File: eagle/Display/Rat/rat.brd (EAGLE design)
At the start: 97.8 x 101.3 mm, 67 parts, among them IC1 4511D, IC2 MEGA128-A, IC3 PCA82C250T, IC4 74LS138D, IC5 74LS138D, IC6 LM3914V, IC7 LM3914V, Q1 18.4320 MHz

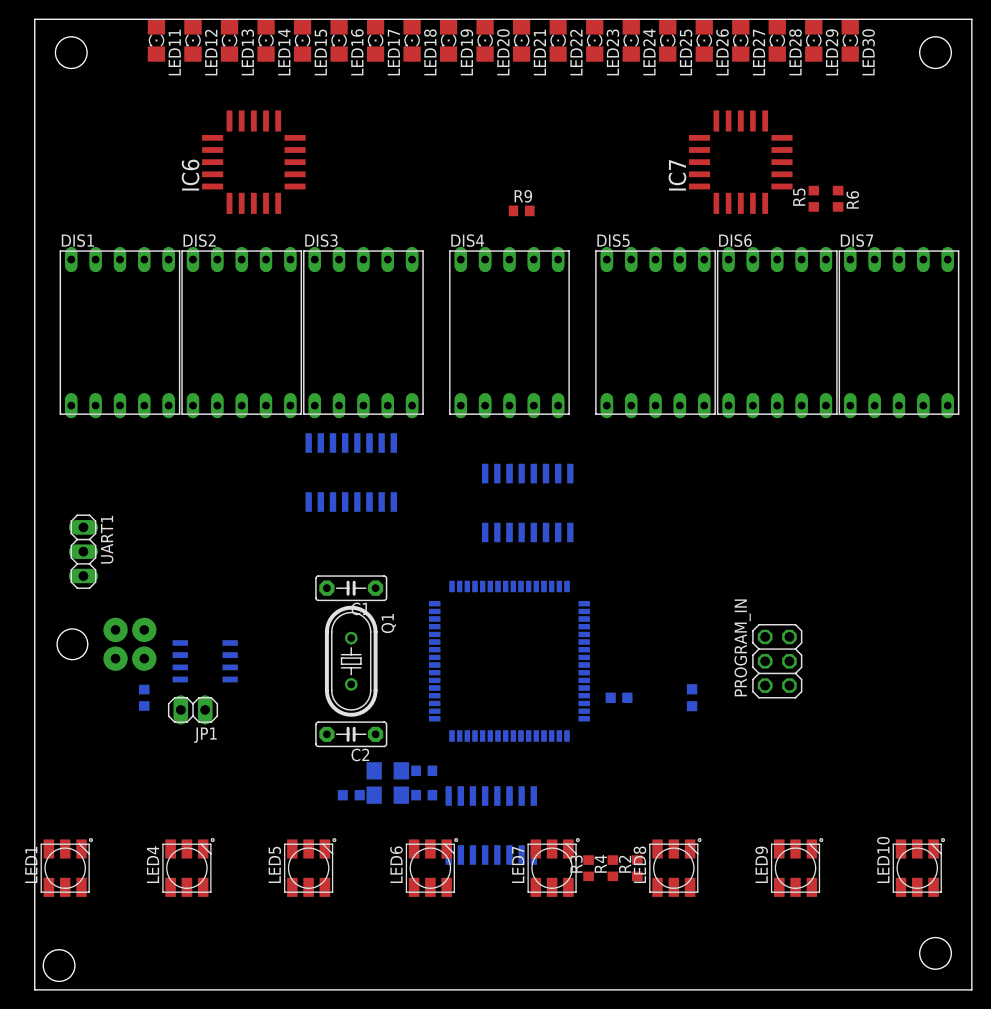
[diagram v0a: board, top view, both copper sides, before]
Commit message: changes to the schematic and board layout
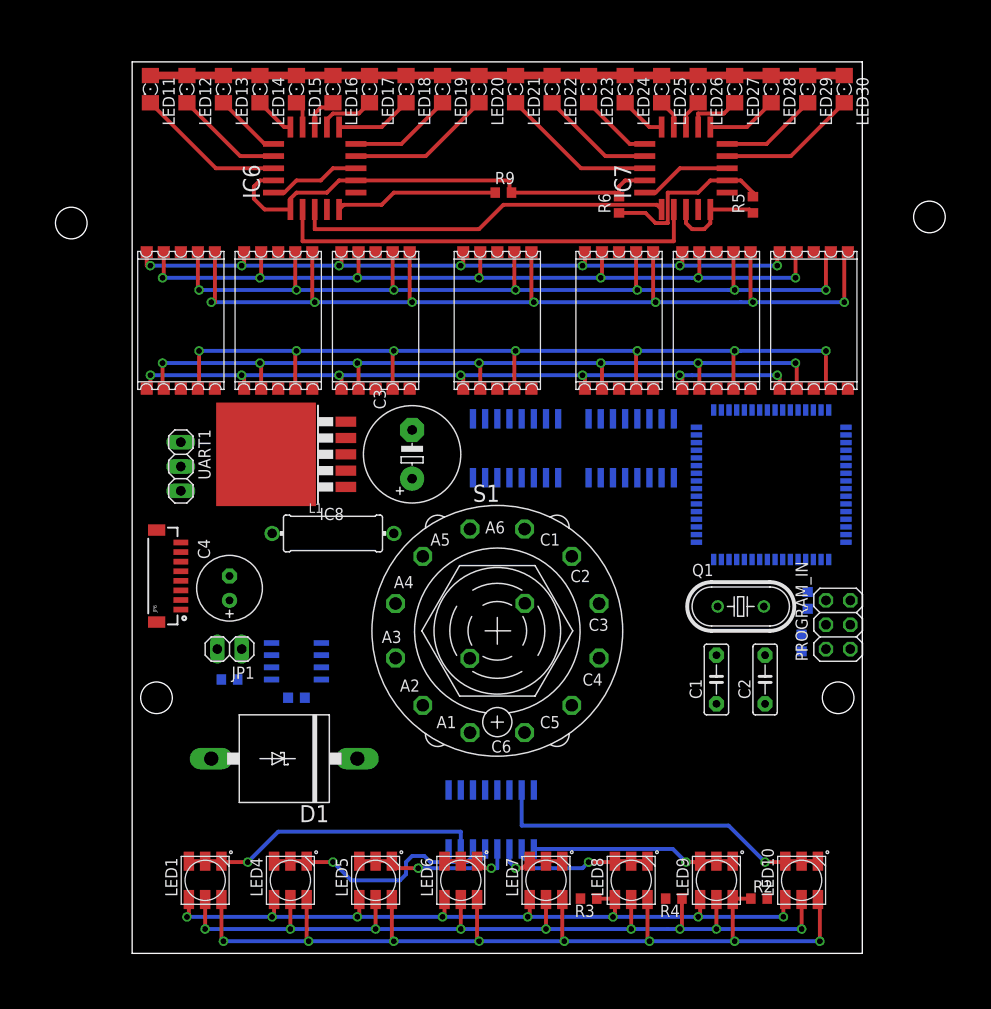
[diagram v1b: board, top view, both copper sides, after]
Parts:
- removed DIS1, DIS2, DIS3, DIS4, DIS5, DIS6, DIS7: HD-H103, display-hp:HDSP-M
- removed LED2, LED3: GREEN, led:1206
- removed R7, R8: 200, rcl:R0603
- removed U$1: MICROFIT4, UNICORN:MICROFIT4SOCK
- added C3: 680 uf, rcl:E5-10,5
- added C4: 220 uf, rcl:E2,5-7
- added D1: 1n5824, diode:P6T15
- added IC8: (no value), linear:TO263-5
- added JP6: (no value), SparkFun-Connectors:BM08B-SRSS-TB
- added L1: 33 uf, rcl:TFI0410
- added S1: (no value), switch:CK102X06
- added U$2, U$3, U$4, U$5, U$6, U$7, U$8: REDSEVENSEGMENT, red_segment:REDSEGMENT
- moved C2 43.6 mm to (95.2, 41.3), turned to 90 degrees
- moved Q1 41.0 mm to (92.7, 48.9), turned to 0 degrees
- moved C1 39.3 mm to (90.2, 41.3), turned to 90 degrees
- moved IC2 32.9 mm to (95.9, 61.6), turned to 0 degrees
- moved JP3 29.7 mm to (31.8, 39.4)
- moved JP2 28.5 mm to (102.9, 39.4)
- moved R6 22.9 mm to (80.0, 90.8), turned to 90 degrees
- moved C19 22.2 mm to (99.7, 49.5), turned to 270 degrees
- moved JP5 17.8 mm to (22.9, 88.9)
- moved IC4 17.3 mm to (69.2, 65.4)
- moved JP4 17.2 mm to (112.4, 89.5)
- moved LED1 14.7 mm to (36.8, 20.3)
- moved UART1 13.5 mm to (34.3, 63.5)
- moved R2 13.1 mm to (94.6, 18.4), turned to 0 degrees
- moved C6 12.8 mm to (99.1, 45.1)
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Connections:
- removed net N$11: LED3.A, R7.1
- removed net N$4: IC2.16, R8.2
- removed net N$5: IC2.15, R7.2
- removed net N$7: LED2.A, R8.1
- new net N$45: D1.C, IC8.2, L1.1
- new net VCC: C3.+, IC8.1, JP6.5, JP6.6
- net +5V: now also C4.+, IC8.4, L1.2
- net CANJUMP1: now also JP6.1; no longer U$1.PIN1
- net N$12: now also U$2.D, U$3.D, U$4.D, U$5.D, U$6.D, U$7.D, U$8.D; no longer DIS1.2, DIS2.2, DIS3.2, DIS4.2, DIS5.2, DIS6.2, DIS7.2
- net N$13: now also U$2.E, U$3.E, U$4.E, U$5.E, U$6.E, U$7.E, U$8.E; no longer DIS1.1, DIS2.1, DIS3.1, DIS4.1, DIS5.1, DIS6.1, DIS7.1
- net N$14: now also U$2.F, U$3.F, U$4.F, U$5.F, U$6.F, U$7.F, U$8.F; no longer DIS1.9, DIS2.9, DIS3.9, DIS4.9, DIS5.9, DIS6.9, DIS7.9
- net N$15: now also U$2.G, U$3.G, U$4.G, U$5.G, U$6.G, U$7.G, U$8.G; no longer DIS1.10, DIS2.10, DIS3.10, DIS4.10, DIS5.10, DIS6.10, DIS7.10
- net N$16: now also U$2.GN, U$2.GND; no longer DIS1.3, DIS1.8
- net N$17: now also U$3.GN, U$3.GND; no longer DIS2.3, DIS2.8
- net N$18: now also U$4.GN, U$4.GND; no longer DIS3.3, DIS3.8
- net N$19: now also U$5.GN, U$5.GND; no longer DIS4.3, DIS4.8
- net N$20: now also U$6.GN, U$6.GND; no longer DIS5.3, DIS5.8
- net N$21: now also U$7.GN, U$7.GND; no longer DIS6.3, DIS6.8
- net N$22: now also U$8.GN, U$8.GND; no longer DIS7.3, DIS7.8
- net N$3: now also U$2.A, U$3.A, U$4.A, U$5.A, U$6.A, U$7.A, U$8.A; no longer DIS1.7, DIS2.7, DIS3.7, DIS4.7, DIS5.7, DIS6.7, DIS7.7
- net N$51: now also JP6.2; no longer U$1.PIN2
- net N$6: now also U$2.B, U$3.B, U$4.B, U$5.B, U$6.B, U$7.B, U$8.B; no longer DIS1.6, DIS2.6, DIS3.6, DIS4.6, DIS5.6, DIS6.6, DIS7.6
- net N$8: now also U$2.C, U$3.C, U$4.C, U$5.C, U$6.C, U$7.C, U$8.C; no longer DIS1.4, DIS2.4, DIS3.4, DIS4.4, DIS5.4, DIS6.4, DIS7.4
- net PE: now also C3.-, C4.-, D1.A, IC8.3, IC8.5, IC8.6, JP6.3, JP6.4; no longer LED2.C, LED3.C, U$1.PIN3, U$1.PIN4
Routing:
- net N$6: track 0.00 -> 104.5 mm, vias 0 -> 7
- net N$32: track 0.00 -> 99.6 mm, vias 0 -> 8
- net N$8: track 0.00 -> 94.2 mm, vias 0 -> 7
- net N$3: track 0.00 -> 94.2 mm, vias 0 -> 7
- net N$30: track 0.00 -> 90.1 mm, vias 0 -> 9
- net N$12: track 0.00 -> 85.6 mm, vias 0 -> 7
- net N$14: track 0.00 -> 85.6 mm, vias 0 -> 7
- net N$31: track 0.00 -> 79.3 mm, vias 0 -> 8
- net N$15: track 0.00 -> 77.1 mm, vias 0 -> 7
- net N$13: track 0.00 -> 77.1 mm, vias 0 -> 7
- net N$69: track 0.00 -> 72.4 mm
- net PE: track 0.00 -> 49.3 mm
- net N$73: track 0.00 -> 45.4 mm
- net N$72: track 0.00 -> 39.5 mm
- net N$40: track 0.00 -> 36.2 mm, vias 0 -> 1
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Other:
- board size 97.8 x 101.3 mm -> 76.2 x 93 mm

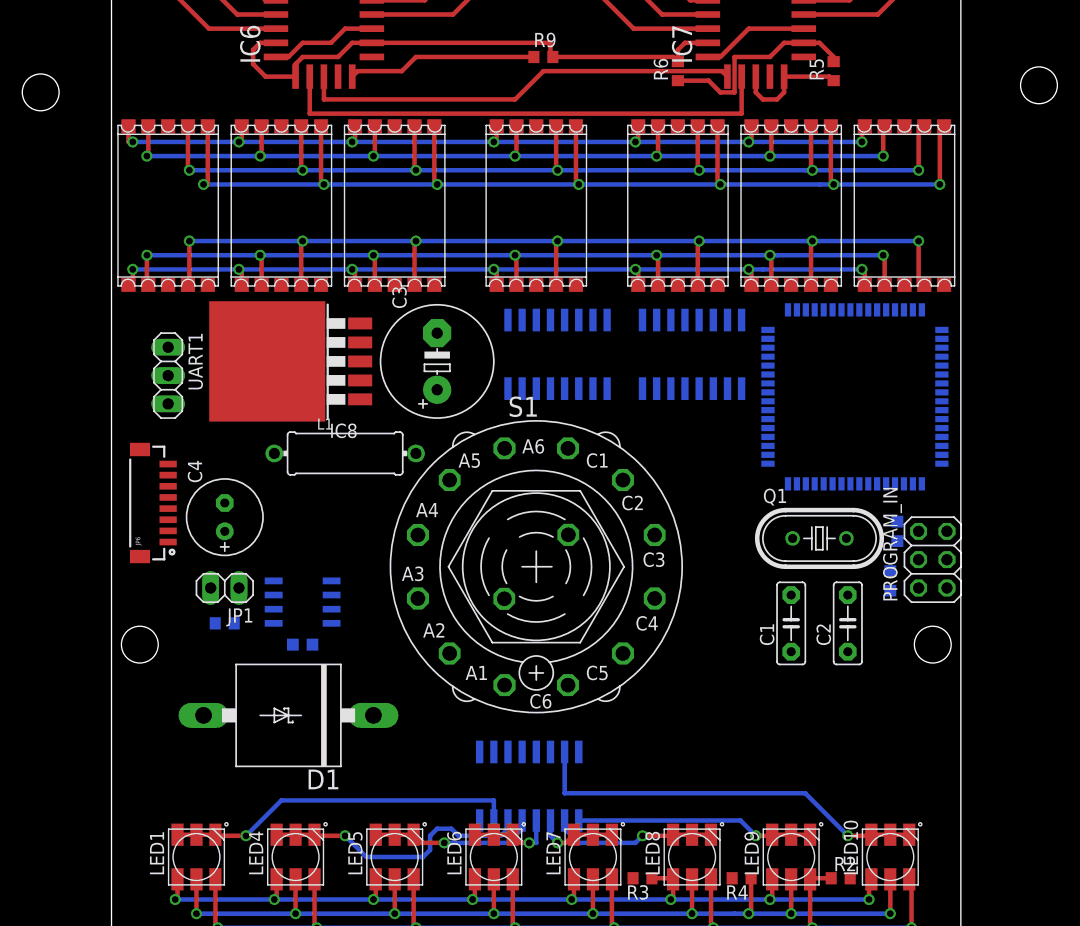
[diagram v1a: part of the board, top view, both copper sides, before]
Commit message: more changes to steering wheel display
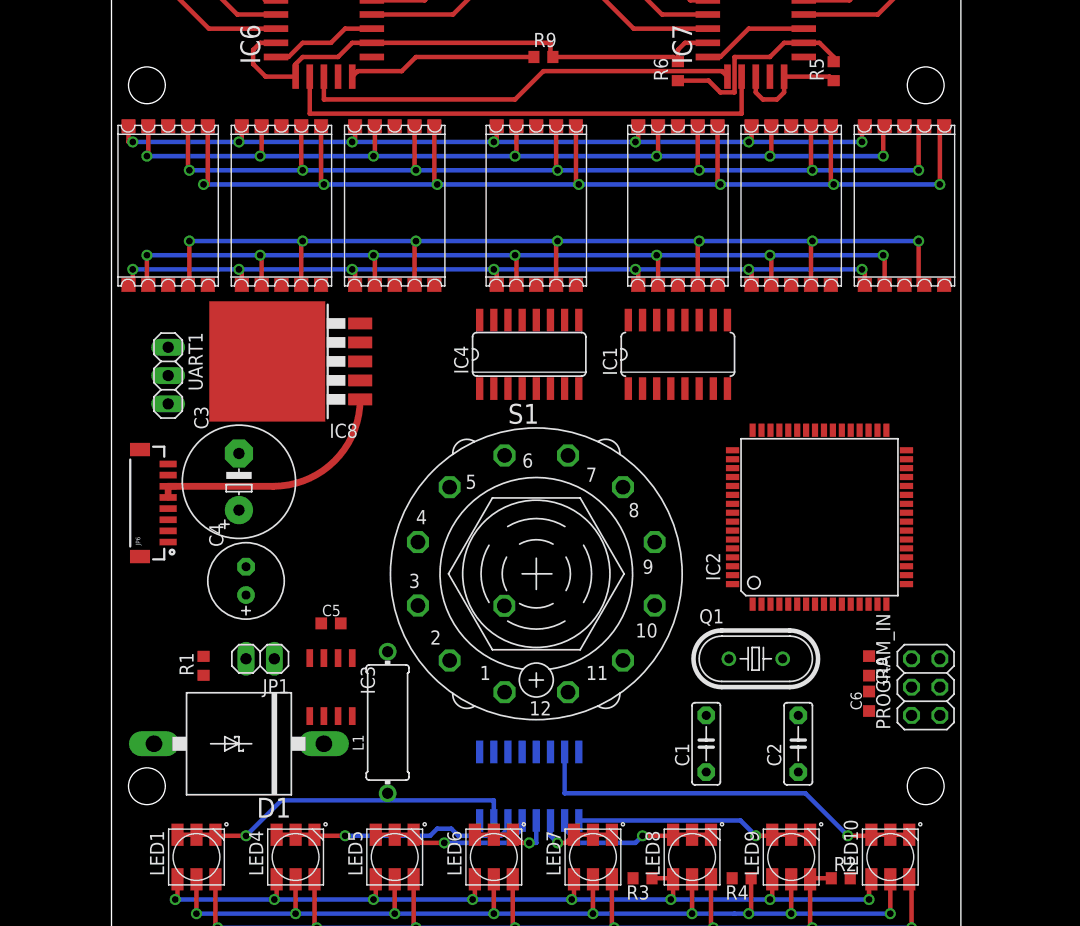
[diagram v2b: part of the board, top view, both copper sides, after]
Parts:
- L1: value 33 uf -> 33 uh
- S1: device switch:CK102X06 -> switch:CK101X12
- moved L1 24.4 mm to (54.0, 32.4), turned to 90 degrees
- moved C3 20.8 mm to (40.6, 54.0)
- moved C1 13.2 mm to (82.5, 30.5)
- moved JP2 12.7 mm to (102.2, 26.7)
- moved JP3 12.7 mm to (32.4, 26.7)
- moved C19 12.3 mm to (97.2, 37.5), flipped to the top
- moved Q1 12.2 mm to (87.0, 38.1)
- moved C2 11.7 mm to (90.8, 30.5)
- moved PROGRAM_IN 11.4 mm to (102.2, 35.6)
- moved IC2 11.3 mm to (92.7, 50.8), flipped to the top, turned to 90 degrees
- moved C6 11.0 mm to (97.2, 34.3), flipped to the top
- moved JP4 10.2 mm to (102.2, 89.5)
- moved JP5 9.55 mm to (32.4, 89.5)
- moved IC3 8.03 mm to (48.9, 35.6), flipped to the top, turned to 180 degrees
- moved JP1 7.10 mm to (42.5, 38.1)
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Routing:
- net VCC: track 0.00 -> 21.5 mm
- net N$34: track 24.6 -> 22.3 mm

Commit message: more changes
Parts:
- removed S1: (no value), switch:CK101X12
- moved UART1 205.5 mm to (233.0, 11.4)
- moved JP4 170.7 mm to (271.1, 64.8)
- moved JP2 164.3 mm to (262.3, -10.8)
- moved LED9 164.3 mm to (247.7, -26.7)
- moved LED8 163.1 mm to (237.5, -26.7)
- moved LED7 161.9 mm to (227.3, -26.7)
- moved LED10 161.1 mm to (255.3, -19.1)
- moved LED6 160.7 mm to (217.2, -26.7)
- moved IC1 159.8 mm to (236.2, 31.8)
- moved LED5 159.5 mm to (207.0, -26.7)
- moved LED4 158.3 mm to (196.8, -26.7)
- moved LED1 158.0 mm to (189.9, -19.1)
- moved IC4 157.9 mm to (221.0, 31.8)
- moved L1 157.7 mm to (208.3, 0.00)
- moved IC5 157.5 mm to (217.8, -17.8)
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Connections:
- removed net N$69: LED11.A, LED12.A, LED13.A, LED14.A, LED15.A, LED16.A, LED17.A, LED18.A, LED19.A, LED20.A, LED21.A, LED22.A, LED23.A, LED24.A, LED25.A, LED26.A, LED27.A, LED28.A, LED29.A, LED30.A
- net +5V: now also LED11.A, LED12.A, LED13.A, LED14.A, LED15.A, LED16.A, LED17.A, LED18.A, LED19.A, LED20.A, LED21.A, LED22.A, LED23.A, LED24.A, LED25.A, LED26.A, LED27.A, LED28.A, LED29.A, LED30.A
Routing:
- net N$6: track 104.5 -> 0.00 mm, vias 7 -> 0
- net N$32: track 99.6 -> 0.00 mm, vias 8 -> 0
- net N$8: track 94.2 -> 0.00 mm, vias 7 -> 0
- net N$3: track 94.2 -> 0.00 mm, vias 7 -> 0
- net N$30: track 90.1 -> 0.00 mm, vias 9 -> 0
- net N$14: track 85.6 -> 0.00 mm, vias 7 -> 0
- net N$12: track 85.6 -> 0.00 mm, vias 7 -> 0
- net N$31: track 79.3 -> 0.00 mm, vias 8 -> 0
- net N$15: track 77.1 -> 0.00 mm, vias 7 -> 0
- net N$13: track 77.1 -> 0.00 mm, vias 7 -> 0
- net N$69: track 72.4 -> 0.00 mm
- net PE: track 49.3 -> 0.00 mm
- net N$73: track 45.4 -> 0.00 mm
- net N$72: track 39.5 -> 0.00 mm
- net N$40: track 36.2 -> 0.00 mm, vias 1 -> 0
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- added copper zone on layer 1, net N$4
- added copper zone on layer 16, net N$5
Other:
- board size 76.2 x 93 mm -> 105.4 x 116.2 mm

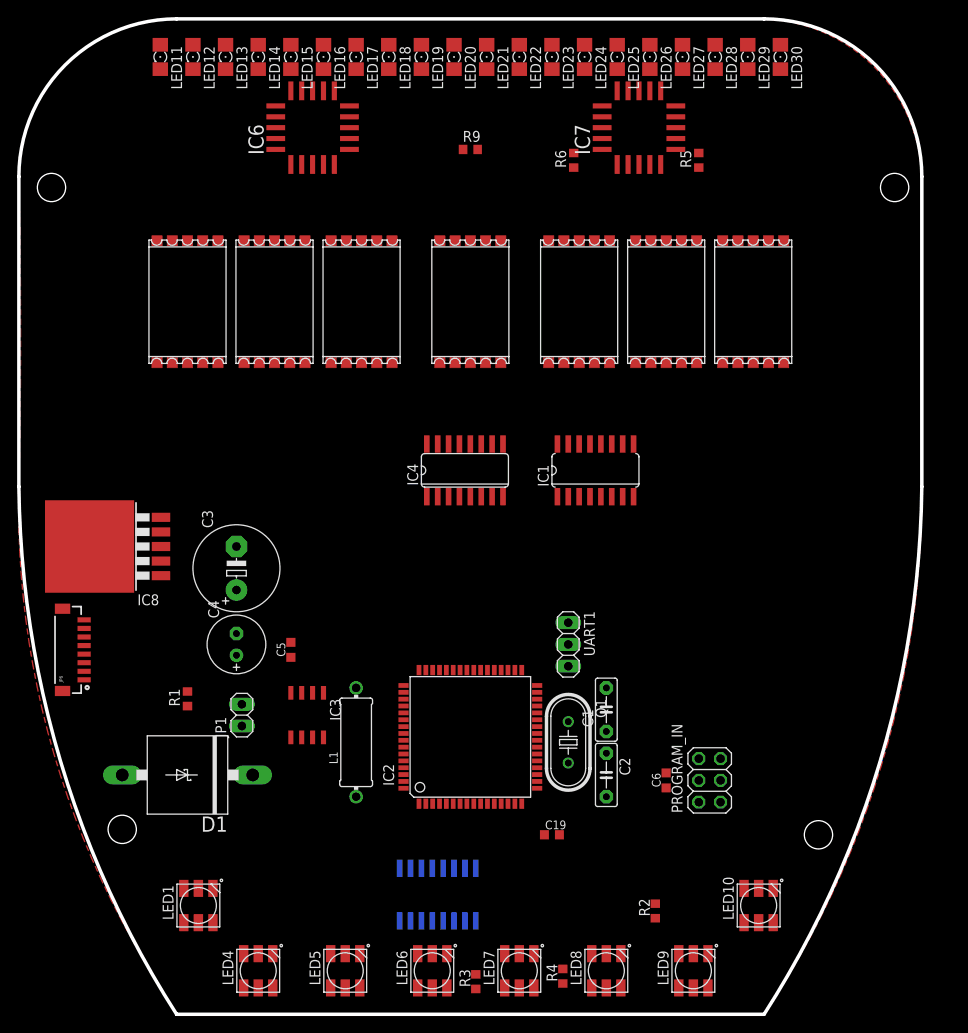
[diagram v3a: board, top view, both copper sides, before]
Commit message: added drill holes for buttons
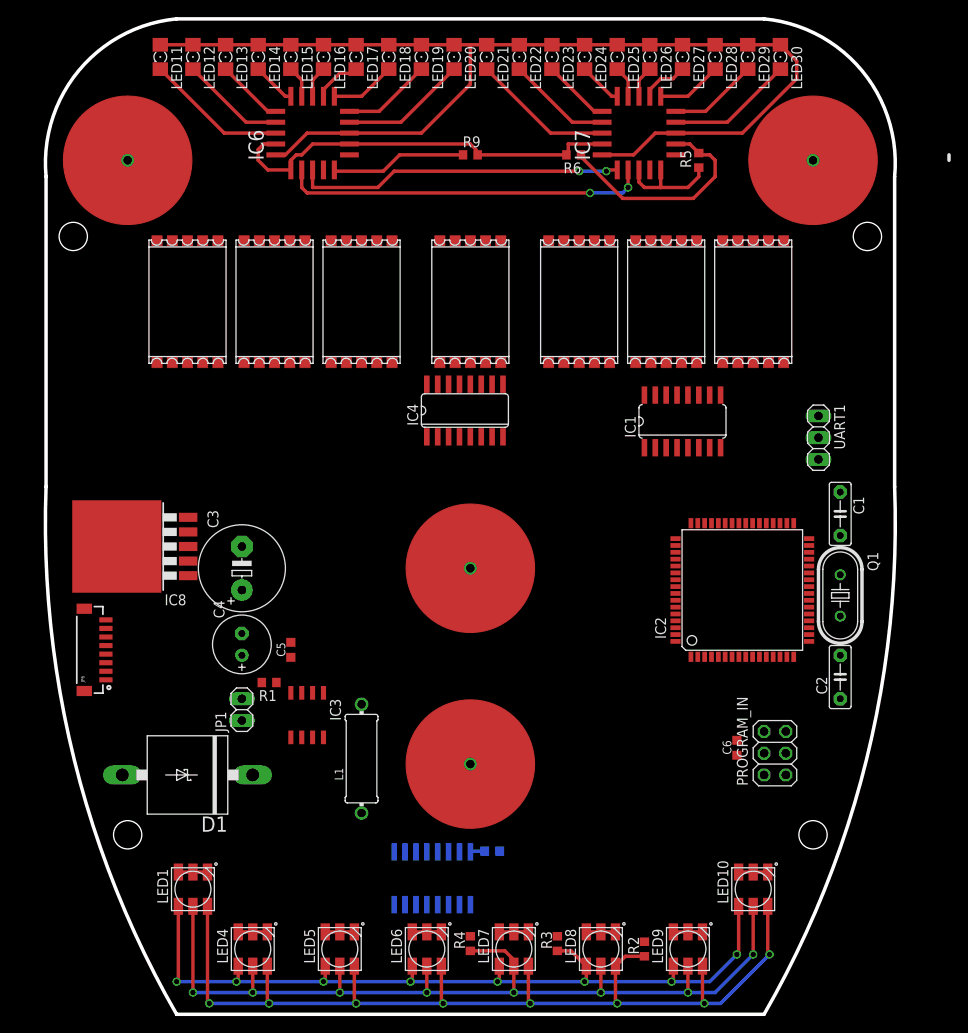
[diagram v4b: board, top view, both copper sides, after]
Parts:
- added U$12, U$13, U$14, U$15: 15MM-DRILLHOLE, 15mm-drillhole:15MM-DRILLHOLE
- moved UART1 37.9 mm to (262.3, 35.6)
- moved Q1 36.1 mm to (264.8, 17.1)
- moved IC2 36.1 mm to (253.4, 17.8)
- moved C1 35.6 mm to (264.8, 26.7), turned to 270 degrees
- moved C2 29.6 mm to (264.8, 7.62), turned to 90 degrees
- moved IC1 11.7 mm to (246.4, 37.5)
- moved R4 11.4 mm to (221.6, -23.5)
- moved R3 10.5 mm to (231.8, -23.5)
- moved R1 9.71 mm to (198.1, 6.99), turned to 180 degrees
- moved C6 9.09 mm to (252.7, -0.64)
- moved PROGRAM_IN 8.26 mm to (257.2, -1.27)
- moved C19 7.24 mm to (224.2, -12.7), flipped to the bottom
- moved IC4 6.98 mm to (221.0, 38.7)
- moved JP4 6.54 mm to (268.0, 59.1)
- moved JP5 6.25 mm to (175.3, 59.1)
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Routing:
- net +5V: track 0.00 -> 134.3 mm
- net N$32: track 0.00 -> 115.4 mm, vias 0 -> 8
- net N$30: track 0.00 -> 107.7 mm, vias 0 -> 8
- net N$31: track 0.00 -> 96.8 mm, vias 0 -> 8
- net PE: track 0.00 -> 49.7 mm
- net N$73: track 0.00 -> 42.7 mm, vias 0 -> 2
- net N$72: track 0.00 -> 38.5 mm, vias 0 -> 2
- net N$75: track 0.00 -> 26.2 mm
- net N$48: track 0.00 -> 16.6 mm
- net N$59: track 0.00 -> 16.6 mm
- net N$76: track 0.00 -> 15.9 mm
- net N$68: track 0.00 -> 14.8 mm
- net N$58: track 0.00 -> 14.8 mm
- net N$74: track 0.00 -> 12.3 mm
- net N$49: track 0.00 -> 12.2 mm
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- removed copper zone on layer 1, net N$4
- removed copper zone on layer 16, net N$5
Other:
- board size 105.4 x 116.2 mm -> 99.2 x 116.2 mm
